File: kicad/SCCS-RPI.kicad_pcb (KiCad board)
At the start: 4 copper layers, 228 x 122 mm, 302 parts, among them J1 Conn_Coaxial, J2 12VDC IN, K1 Relay_SPDT, K2 Relay_SPDT, K3 Relay_SPDT, K4 Relay_SPDT, Q1 IRLR7843, Q10 IRLR7843, Q11 IRLR7843, Q12 IRLR7843, Q13 IRLR7843, Q14 IRLR7843, Q15 IRLR7843, Q16 IRLR7843, Q17 2N7000, Q18 2N7000, Q19 2N7000, Q2 IRLR7843, Q20 2N7000, Q3 IRLR7843, Q4 IRLR7843, Q5 IRLR7843, Q6 IRLR7843, Q7 IRLR7843, Q8 IRLR7843, Q9 IRLR7843, SW1 RESET, SW2 BOOT, SW3 RESET, SW4 BOOT, U1 SN74LVC2T45DCUR, U2 AP64501SP-13, U3 PC817, U4 PC817, U5 PC817, U6 PC817

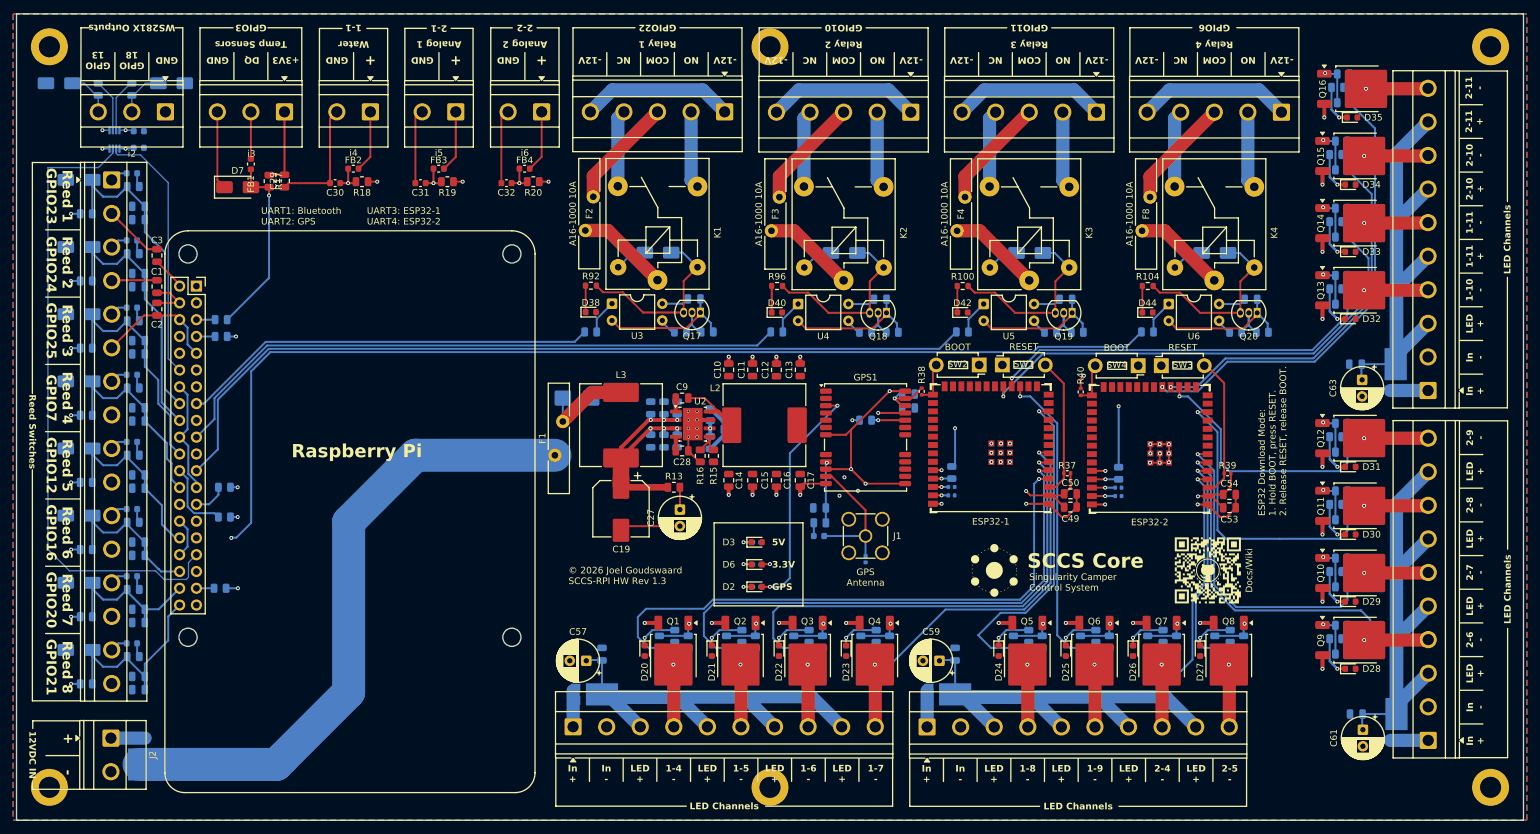
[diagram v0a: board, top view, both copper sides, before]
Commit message: Update SCCS-RPI KiCad design and production files
Split 5V and 3V3 regulation onto dedicated Power sheets with a second
AP64501 buck, extra inductor and passives, update the enclosure
bracket, and regenerate BOM, positions, netlist, gerbers, and
schematics PDF.
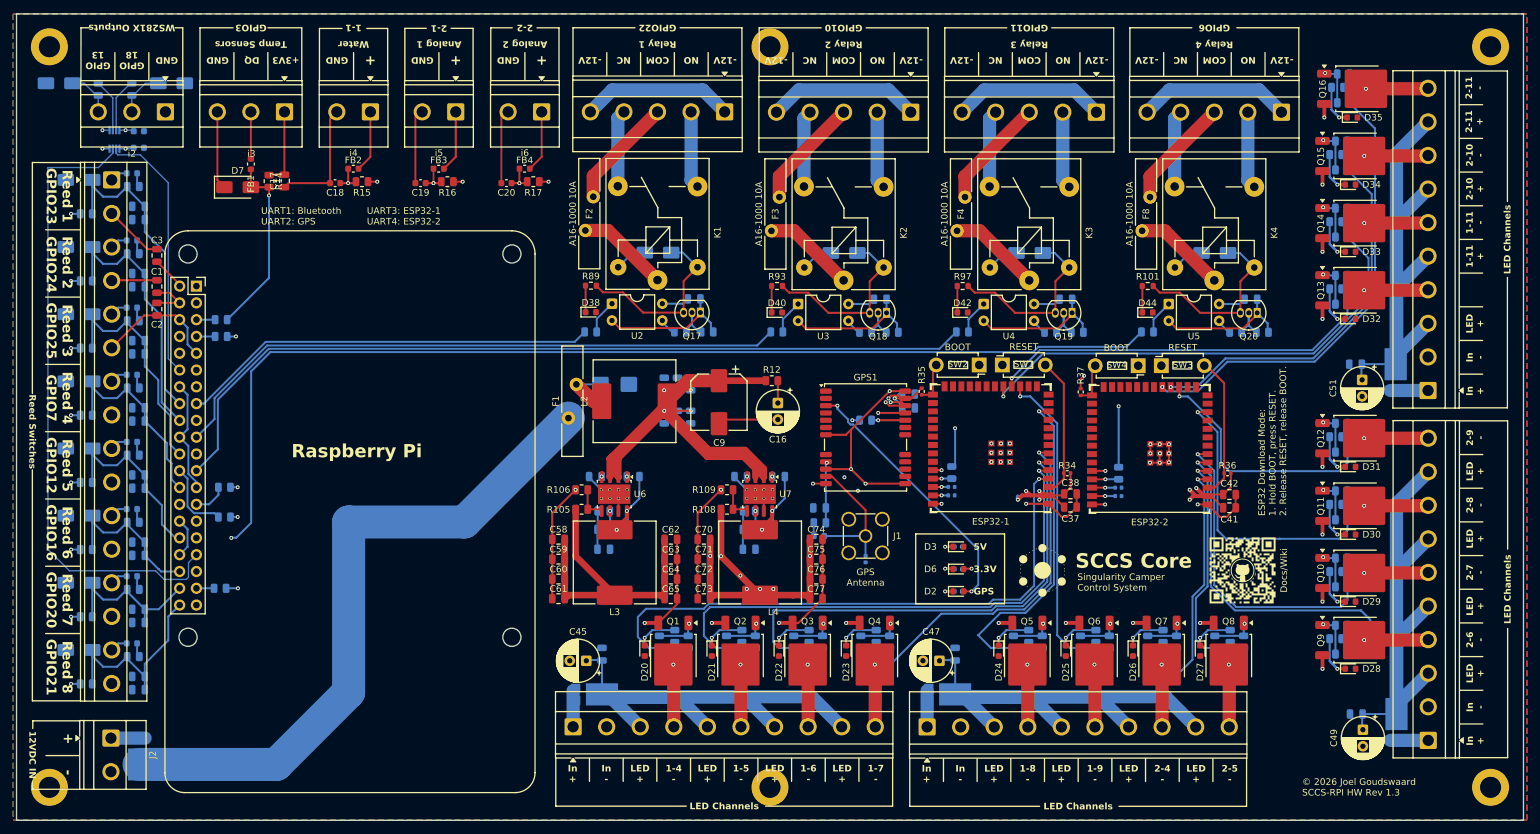
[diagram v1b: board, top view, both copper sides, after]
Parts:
- removed the C10 at (308.3, 179.9)
- removed the C11 at (311.9, 179.9)
- removed the C12 at (315.5, 179.9)
- removed the C13 at (319.1, 179.9)
- removed the C14 at (308.3, 196.6)
- removed the C15 at (311.9, 196.6)
- removed the C16 at (315.5, 196.6)
- removed the C17 at (319.1, 196.6)
- removed the C18 at (308.5, 188.9)
- removed the C26 at (305.5, 190.9)
- removed the C28 at (301.2, 192.1)
- removed the C9 at (301.2, 184.1)
- removed the L2 at (313.7, 188.2)
- removed the R12 at (305.5, 186.6)
- removed the R15 at (306.0, 192.9)
- removed the R16 at (303.9, 192.9)
- removed the U2 at (302.8, 188.1)
- added C57: 0.1uF, Capacitor_SMD:C_0805_2012Metric, B.Cu at (293.8, 196.0)
- added C58: 22uF, Capacitor_SMD:C_0805_2012Metric, F.Cu at (282.5, 205.5)
- added C59: 22uF, Capacitor_SMD:C_0805_2012Metric, F.Cu at (282.5, 208.5)
- added C60: 22uF, Capacitor_SMD:C_0805_2012Metric, F.Cu at (282.5, 211.5)
- added C61: 22uF, Capacitor_SMD:C_0805_2012Metric, F.Cu at (282.5, 214.5)
- added C62: 22uF, Capacitor_SMD:C_0805_2012Metric, F.Cu at (299.5, 205.5)
- added C63: 22uF, Capacitor_SMD:C_0805_2012Metric, F.Cu at (299.5, 208.5)
- added C64: 22uF, Capacitor_SMD:C_0805_2012Metric, F.Cu at (299.5, 211.5)
- added C65: 22uF, Capacitor_SMD:C_0805_2012Metric, F.Cu at (299.5, 214.5)
- added C66: 2.7nF, Capacitor_SMD:C_0805_2012Metric, B.Cu at (289.3, 207.0)
- added C67: 33pF, Capacitor_SMD:C_0805_2012Metric, B.Cu at (289.3, 204.0)
- added C68: 10nF, Capacitor_SMD:C_0805_2012Metric, B.Cu at (288.1, 196.0)
- added C69: 0.1uF, Capacitor_SMD:C_0805_2012Metric, B.Cu at (315.8, 196.0)
- added C70: 22uF, Capacitor_SMD:C_0805_2012Metric, F.Cu at (304.5, 205.5)
- added C71: 22uF, Capacitor_SMD:C_0805_2012Metric, F.Cu at (304.5, 208.5)
- added C72: 22uF, Capacitor_SMD:C_0805_2012Metric, F.Cu at (304.5, 211.5)
- added C73: 22uF, Capacitor_SMD:C_0805_2012Metric, F.Cu at (304.5, 214.5)
- added C74: 22uF, Capacitor_SMD:C_0805_2012Metric, F.Cu at (321.5, 205.5)
- added C75: 22uF, Capacitor_SMD:C_0805_2012Metric, F.Cu at (321.5, 208.5)
- added C76: 22uF, Capacitor_SMD:C_0805_2012Metric, F.Cu at (321.5, 211.5)
- added C77: 22uF, Capacitor_SMD:C_0805_2012Metric, F.Cu at (321.5, 214.5)
- added C78: 2.7nF, Capacitor_SMD:C_0805_2012Metric, B.Cu at (311.3, 207.0)
- added C79: 33pF, Capacitor_SMD:C_0805_2012Metric, B.Cu at (311.3, 204.0)
- added C80: 10nF, Capacitor_SMD:C_0805_2012Metric, B.Cu at (310.1, 196.0)
- added L3: 3.3uH, Inductor_SMD:L_SXN_SMDRI127, F.Cu at (291.0, 209.0)
- added L4: 3.3uH, Inductor_SMD:L_SXN_SMDRI127, F.Cu at (313.0, 209.0)
- added R104: 15.8K, Resistor_SMD:R_0805_2012Metric, B.Cu at (289.3, 201.2)
- added R105: 115K, Resistor_SMD:R_0805_2012Metric, F.Cu at (286.0, 200.9)
- added R106: 22.1K, Resistor_SMD:R_0805_2012Metric, F.Cu at (286.0, 198.0)
- added R107: 15.8K, Resistor_SMD:R_0805_2012Metric, B.Cu at (311.3, 201.2)
- added R108: 100K, Resistor_SMD:R_0805_2012Metric, F.Cu at (308.0, 200.9)
- added R109: 32.4K, Resistor_SMD:R_0805_2012Metric, F.Cu at (308.0, 198.0)
- added U6: AP64501SP-13, Package_SO:SOIC-8-1EP_3.9x4.9mm_P1.27mm_EP2.95x4.9mm_Mask2.71x3.4mm_ThermalVias, F.Cu at (290.9, 198.7)
- added U7: AP64501SP-13, Package_SO:SOIC-8-1EP_3.9x4.9mm_P1.27mm_EP2.95x4.9mm_Mask2.71x3.4mm_ThermalVias, F.Cu at (312.9, 198.7)
- moved D2 30.5 mm to (343.0, 213.4)
- moved D3 30.5 mm to (343.0, 206.6)
- moved D6 30.5 mm to (343.0, 210.0)
- moved R10 30.5 mm to (343.0, 213.4)
- moved R11 30.5 mm to (343.0, 206.6)
- moved R13 30.5 mm to (343.0, 210.0)
- moved C16 21.9 mm to (315.7, 184.9)
- moved C9 21.9 mm to (306.8, 184.8)
- moved R12 21.9 mm to (314.8, 181.5)
- moved G*** 7.28 mm to (355.7, 210.2)
- moved D5 6.06 mm to (291.0, 182.1)
- moved F1 5.98 mm to (284.0, 187.2)
- moved G*** 5.25 mm to (386.0, 210.2)
- moved C10 4.16 mm to (302.5, 182.0)
- moved C11 4.16 mm to (302.5, 187.0)
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- renumbered C20 to C10, C21 to C11, C22 to C12, C23 to C13, C24 to C14, C25 to C15, C27 to C16, C29 to C17, C30 to C18, C31 to C19, C32 to C20, C33 to C21, C34 to C22, C35 to C23, C36 to C24, C37 to C25, C38 to C26, C39 to C27, C40 to C28, C41 to C29, C42 to C30, C43 to C31, C44 to C32, C45 to C33, C46 to C34, C47 to C35, C48 to C36, C49 to C37, C50 to C38, C51 to C39, C52 to C40, C53 to C41, C54 to C42, C55 to C43, C56 to C44, C57 to C45, C58 to C46, C59 to C47, C60 to C48, C61 to C49, C62 to C50, C63 to C51, C64 to C52, C65 to C53, C66 to C54, C67 to C55, C68 to C56, C19 to C9, L3 to L2, R103 to R100, R104 to R101, R105 to R102, R106 to R103, R13 to R12, R14 to R13, R17 to R14, R18 to R15, R19 to R16, R20 to R17, R21 to R18, R22 to R19, R23 to R20, R24 to R21, R25 to R22, R26 to R23, R27 to R24, R28 to R25, R29 to R26, R30 to R27, R31 to R28, R32 to R29, R33 to R30, R34 to R31, R35 to R32, R36 to R33, R37 to R34, R38 to R35, R39 to R36, R40 to R37, R41 to R38, R42 to R39, R43 to R40, R44 to R41, R45 to R42, R46 to R43, R47 to R44, R48 to R45, R49 to R46, R50 to R47, R51 to R48, R52 to R49, R53 to R50, R54 to R51, R55 to R52, R56 to R53, R57 to R54, R58 to R55, R59 to R56, R60 to R57, R61 to R58, R62 to R59, R63 to R60, R64 to R61, R65 to R62, R66 to R63, R67 to R64, R68 to R65, R69 to R66, R70 to R67, R71 to R68, R72 to R69, R73 to R70, R74 to R71, R75 to R72, R76 to R73, R77 to R74, R78 to R75, R79 to R76, R80 to R77, R81 to R78, R82 to R79, R83 to R80, R84 to R81, R85 to R82, R86 to R83, R87 to R84, R88 to R85, R89 to R86, R90 to R87, R91 to R88, R92 to R89, R93 to R90, R94 to R91, R95 to R92, R96 to R93, R97 to R94, R98 to R95, R99 to R96, R100 to R97, R101 to R98, R102 to R99, U3 to U2, U4 to U3, U5 to U4, U6 to U5
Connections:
- net Net-(U2-EN) renamed /Power - 3V3/Power_in
- PI1 pad 1: +3V3 -> unconnected-(PI1-Pin_1-Pad1)
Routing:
- net /Power - 3V3/Power_in: track 38.7 -> 106.9 mm, vias 6 -> 4
- net +3V3: track 70.1 -> 138.3 mm, vias 19 -> 34
- net GND: track 330.5 -> 385.0 mm, vias 52 -> 46
- net +5V: track 51.2 -> 100.2 mm
- net Net-(U7-SW): track 0.00 -> 13.1 mm, vias 0 -> 2
- net Net-(U6-SW): track 0.00 -> 13.1 mm, vias 0 -> 2
- net Net-(U2-SW): track 9.54 -> 0.00 mm
- net Net-(C18-Pad2): track 7.81 -> 0.00 mm
- net Net-(C78-Pad2): track 0.00 -> 5.91 mm
- net Net-(C66-Pad2): track 0.00 -> 5.91 mm
- net Net-(U7-FB): track 0.00 -> 5.17 mm
- net Net-(U6-FB): track 0.00 -> 5.17 mm
- net Net-(D2-A): track 35.6 -> 40.5 mm
- net Net-(D5-K): track 14.2 -> 9.33 mm
- net Net-(U2-FB): track 4.80 -> 0.00 mm
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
